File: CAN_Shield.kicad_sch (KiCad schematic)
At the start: 17 parts, among them J1 GPIO, U1 MX128-5.08-09P-GN01-CU-Y-A, U2 MCP2515T-I/SO, U3 MX128-5.08-10P-GN01-CU-Y-A, U4 SN65HVD230DR, X1 X322516MLB4SI

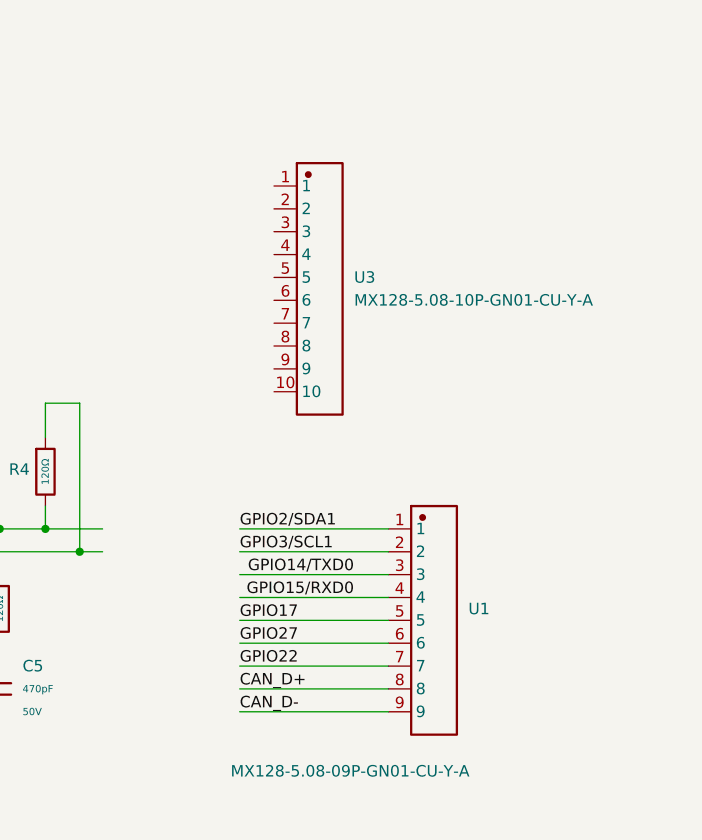
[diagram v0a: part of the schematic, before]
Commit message: change from gpio to gnd at screw terminal and add copper pour for gnd
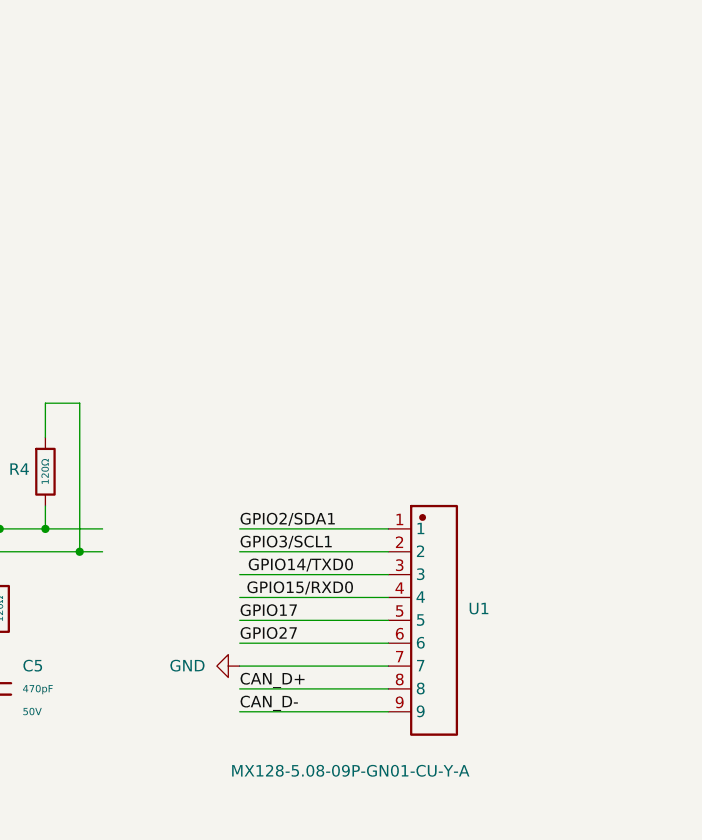
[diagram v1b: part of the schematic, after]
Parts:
- removed U3: MX128-5.08-10P-GN01-CU-Y-A, symbol ImportSymbol:MX128-5.08-10P-GN01-CU-Y-A
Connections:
- net GND: now also U1.7
- net GPIO22: no longer U1.7
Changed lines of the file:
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@@
 	(wire
 		(pts
-			(xy 224.79 139.7) (xy 241.3 139.7)
-		)
-		(stroke
-			(width 0)
-			(type default)
-		)
-	)
-	(wire
-		(pts
 			(xy 203.2 114.3) (xy 203.2 110.49)
 		)
@@
 	(wire
 		(pts
+			(xy 224.79 139.7) (xy 241.3 139.7)
+		)
+		(stroke
+			(width 0)
+			(type default)
+		)
+	)
+	(wire
+		(pts
 			(xy 49.53 44.45) (xy 52.07 44.45)
 		)
@@
 		)
 	)
-	(label "GPIO22"
-		(at 224.79 139.7 0)
-		(effects
-			(font
-				(size 1.27 1.27)
-			)
-			(justify left bottom)
-		)
-	)
 	(label "GPIO23"
 		(at 91.44 52.07 180)
@@
 	)
 	(symbol
+		(lib_name "GND_4")
+		(lib_id "power:GND")
+		(at 224.79 139.7 270)
+		(unit 1)
+		(exclude_from_sim no)
+		(in_bom yes)
+		(on_board yes)
+		(dnp no)
+		(fields_autoplaced yes)
+		(property "Reference" "#PWR6"
+			(at 218.44 139.7 0)
+			(effects
+				(font
+					(size 1.27 1.27)
+				)
+				(hide yes)
+			)
+		)
+		(property "Value" "GND"
+			(at 220.98 139.6999 90)
+			(effects
+				(font
+					(size 1.27 1.27)
+				)
+				(justify right)
+			)
+		)
+		(property "Footprint" ""
+			(at 224.79 139.7 0)
+			(effects
+				(font
+					(size 1.27 1.27)
+				)
+				(hide yes)
+			)
+		)
+		(property "Datasheet" ""
+			(at 224.79 139.7 0)
+			(effects
+				(font
+					(size 1.27 1.27)
+				)
+				(hide yes)
+			)
+		)
+		(property "Description" "Power symbol creates a global label with name \"GND\" , ground"
+			(at 224.79 139.7 0)
+			(effects
+				(font
+					(size 1.27 1.27)
+				)
+				(hide yes)
+			)
+		)
+		(pin "1"
+		)
+		(instances
+			(project "CAN_Shield"
+				(path "/e63e39d7-6ac0-4ffd-8aa3-1841a4541b55"
+					(reference "#PWR6")
+					(unit 1)
+				)
+			)
+		)
+	)
+	(symbol
 		(lib_name "GND_1")
 		(lib_id "power:GND")
@@
 					(unit 1)
 				)
-			)
-		)
-	)
-	(symbol
-		(lib_id "ImportSymbol:MX128-5.08-10P-GN01-CU-Y-A")
-		(at 233.68 97.79 0)
-		(unit 1)
-		(exclude_from_sim no)
-		(in_bom yes)
-		(on_board yes)
-		(dnp no)
-		(fields_autoplaced yes)
-		(property "Reference" "U3"
-			(at 237.49 96.5199 0)
-			(effects
-				(font
-					(size 1.27 1.27)
-				)
-				(justify left)
-			)
-		)
-		(property "Value" "MX128-5.08-10P-GN01-CU-Y-A"
-			(at 237.49 99.0599 0)
-			(effects
-				(font
-					(size 1.27 1.27)
-				)
-				(justify left)
-			)
-		)
-		(property "Footprint" ""
-			(at 233.68 97.79 0)
-			(effects
-				(font
-					(size 1.27 1.27)
-				)
-				(hide yes)
-			)
-		)
-		(property "Datasheet" ""
-			(at 233.68 97.79 0)
-			(effects
-				(font
-					(size 1.27 1.27)
-				)
-				(hide yes)
-			)
-		)
-		(property "Description" ""
-			(at 233.68 97.79 0)
-			(effects
-				(font
-					(size 1.27 1.27)
-				)
-				(hide yes)
-			)
-		)
-		(property "Manufacturer Part" "MX128-5.08-10P-GN01-Cu-Y-A"
-			(at 233.68 97.79 0)
-			(effects
-				(font
-					(size 1.27 1.27)
-				)
-				(hide yes)
-			)
-		)
-		(property "Manufacturer" "MAX(迈旭)"
-			(at 233.68 97.79 0)
-			(effects
-				(font
-					(size 1.27 1.27)
-				)
-				(hide yes)
-			)
-		)
-		(property "Supplier Part" "C5290383"
-			(at 233.68 97.79 0)
-			(effects
-				(font
-					(size 1.27 1.27)
-				)
-				(hide yes)
-			)
-		)
-		(property "Supplier" "LCSC"
-			(at 233.68 97.79 0)
-			(effects
-				(font
-					(size 1.27 1.27)
-				)
-				(hide yes)
-			)
-		)
-		(pin "3"
-		)
-		(pin "10"
-		)
-		(pin "6"
-		)
-		(pin "1"
-		)
-		(pin "2"
-		)
-		(pin "9"
-		)
-		(pin "5"
-		)
-		(pin "4"
-		)
-		(pin "7"
-		)
-		(pin "8"
-		)
-		(instances
-			(project ""
-				(path "/e63e39d7-6ac0-4ffd-8aa3-1841a4541b55"
-					(reference "U3")
-					(unit 1)
-				)

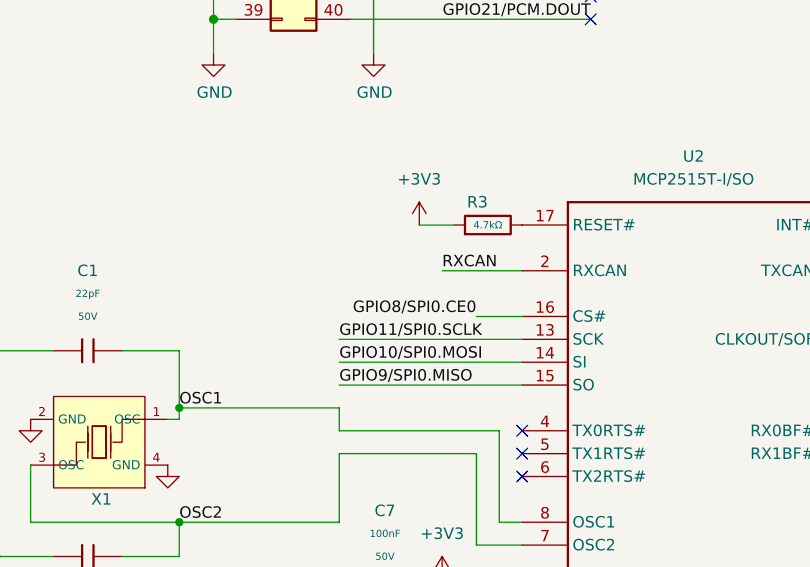
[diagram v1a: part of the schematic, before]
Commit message: change can diff pair trace width to 0.35 mm get 133ohm zdiff
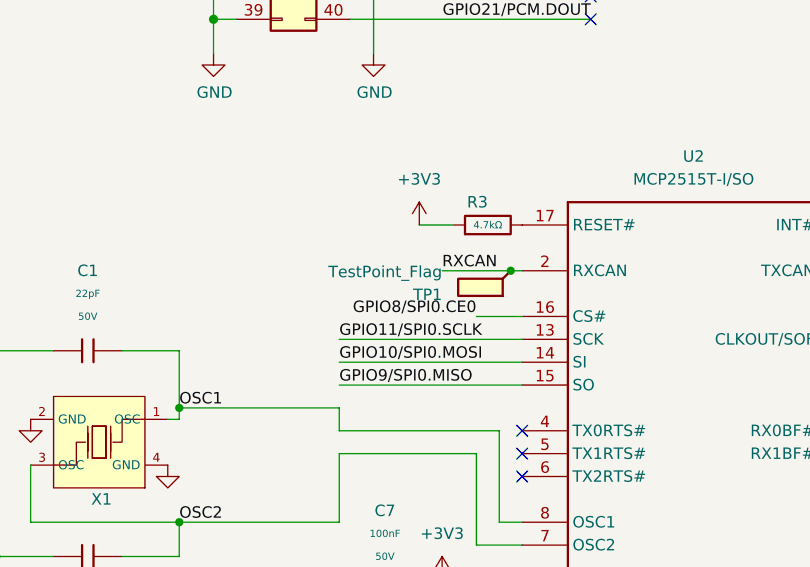
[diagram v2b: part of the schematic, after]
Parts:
- added TP1: TestPoint_Flag, TestPoint:TestPoint_Pad_3.0x3.0mm, symbol Connector:TestPoint_Flag
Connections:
- net RXCAN: now also TP1.1
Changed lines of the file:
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@@
 	)
 	(junction
+		(at 82.55 110.49)
+		(diameter 0)
+		(color 0 0 0 0)
+	)
+	(junction
 		(at 49.53 82.55)
 		(diameter 1.016)
@@
 	(wire
 		(pts
+			(xy 82.55 110.49) (xy 83.82 110.49)
+		)
+		(stroke
+			(width 0)
+			(type default)
+		)
+	)
+	(wire
+		(pts
 			(xy 46.99 19.05) (xy 46.99 34.29)
 		)
@@
 	(wire
 		(pts
-			(xy 74.93 110.49) (xy 83.82 110.49)
+			(xy 74.93 110.49) (xy 82.55 110.49)
 		)
 		(stroke
@@
 					(unit 1)
 				)
+			)
+		)
+	)
+	(symbol
+		(lib_id "Connector:TestPoint_Flag")
+		(at 82.55 110.49 180)
+		(unit 1)
+		(exclude_from_sim no)
+		(in_bom yes)
+		(on_board yes)
+		(dnp no)
+		(property "Reference" "TP1"
+			(at 74.93 113.1571 0)
+			(effects
+				(font
+					(size 1.27 1.27)
+				)
+				(justify left)
+			)
+		)
+		(property "Value" "TestPoint_Flag"
+			(at 74.93 110.6171 0)
+			(effects
+				(font
+					(size 1.27 1.27)
+				)
+				(justify left)
+			)
+		)
+		(property "Footprint" "TestPoint:TestPoint_Pad_3.0x3.0mm"
+			(at 77.47 110.49 0)
+			(effects
+				(font
+					(size 1.27 1.27)
+				)
+				(hide yes)
+			)
+		)
+		(property "Datasheet" "~"
+			(at 77.47 110.49 0)
+			(effects
+				(font
+					(size 1.27 1.27)
+				)
+				(hide yes)
+			)
+		)
+		(property "Description" "test point (alternative flag-style design)"
+			(at 82.55 110.49 0)
+			(effects
+				(font
+					(size 1.27 1.27)
+				)
+				(hide yes)
+			)
+		)
+		(pin "1"
+		)
+		(instances
+			(project ""
+				(path "/e63e39d7-6ac0-4ffd-8aa3-1841a4541b55"
+					(reference "TP1")
+					(unit 1)
+				)

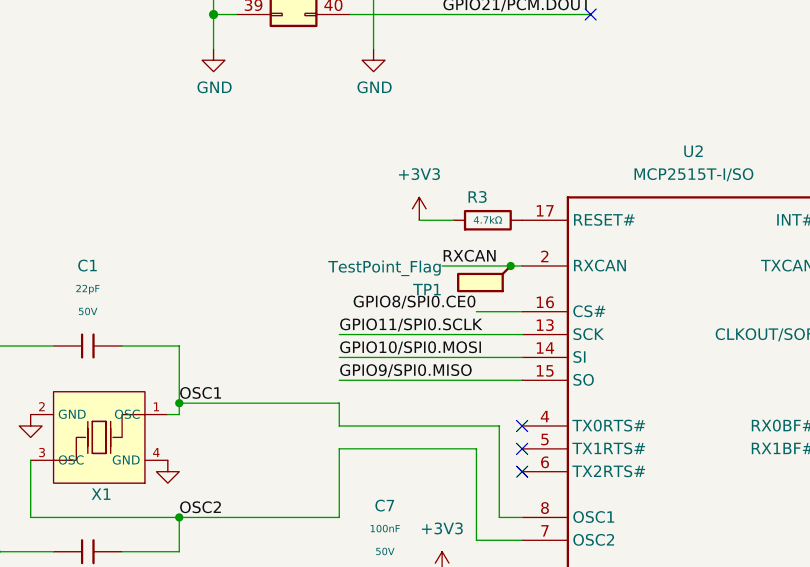
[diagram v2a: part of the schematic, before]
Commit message: tune CAN diff pair skew
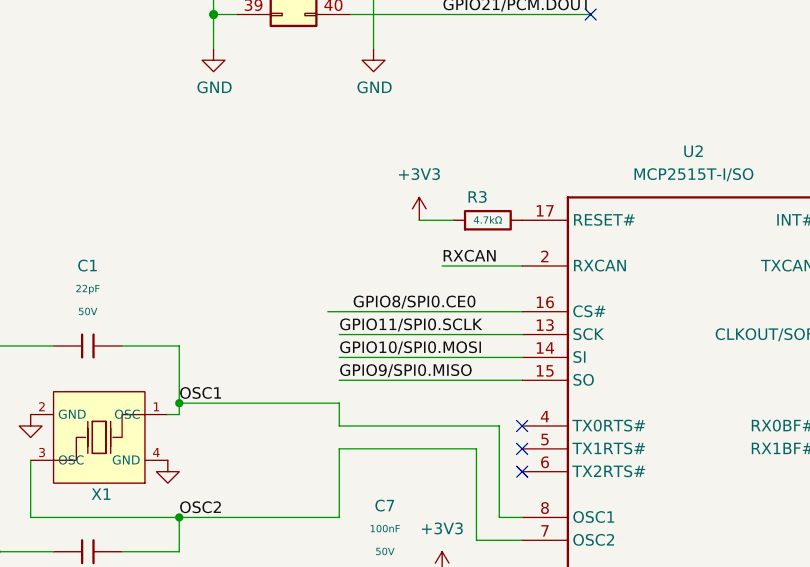
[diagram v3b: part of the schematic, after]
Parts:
- removed TP1: TestPoint_Flag, TestPoint:TestPoint_Pad_3.0x3.0mm, symbol Connector:TestPoint_Flag
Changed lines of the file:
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@@
 	)
 	(junction
-		(at 82.55 110.49)
-		(diameter 0)
-		(color 0 0 0 0)
-	)
-	(junction
 		(at 49.53 82.55)
 		(diameter 1.016)
@@
 	(wire
 		(pts
-			(xy 67.31 69.85) (xy 67.31 74.93)
+			(xy 121.92 110.49) (xy 125.73 110.49)
 		)
 		(stroke
 			(width 0)
-			(type solid)
+			(type default)
 		)
 	)
 	(wire
 		(pts
-			(xy 224.79 137.16) (xy 241.3 137.16)
+			(xy 67.31 69.85) (xy 67.31 74.93)
 		)
 		(stroke
 			(width 0)
-			(type default)
+			(type solid)
 		)
 	)
 	(wire
 		(pts
-			(xy 82.55 110.49) (xy 83.82 110.49)
+			(xy 224.79 137.16) (xy 241.3 137.16)
 		)
 		(stroke
@@
 	(wire
 		(pts
-			(xy 74.93 110.49) (xy 82.55 110.49)
+			(xy 74.93 110.49) (xy 83.82 110.49)
 		)
 		(stroke
@@
 	(wire
 		(pts
-			(xy 121.92 110.49) (xy 125.73 110.49)
-		)
-		(stroke
-			(width 0)
-			(type default)
-		)
-	)
-	(wire
-		(pts
 			(xy 22.86 41.91) (xy 52.07 41.91)
 		)
@@
 	(wire
 		(pts
-			(xy 78.74 115.57) (xy 83.82 115.57)
-		)
-		(stroke
-			(width 0)
-			(type default)
-		)
-	)
-	(wire
-		(pts
 			(xy 22.86 72.39) (xy 52.07 72.39)
 		)
@@
 	(wire
 		(pts
+			(xy 62.23 115.57) (xy 83.82 115.57)
+		)
+		(stroke
+			(width 0)
+			(type default)
+		)
+	)
+	(wire
+		(pts
 			(xy 198.12 137.16) (xy 198.12 138.43)
 		)
@@
 					(unit 1)
 				)
-			)
-		)
-	)
-	(symbol
-		(lib_id "Connector:TestPoint_Flag")
-		(at 82.55 110.49 180)
-		(unit 1)
-		(exclude_from_sim no)
-		(in_bom yes)
-		(on_board yes)
-		(dnp no)
-		(property "Reference" "TP1"
-			(at 74.93 113.1571 0)
-			(effects
-				(font
-					(size 1.27 1.27)
-				)
-				(justify left)
-			)
-		)
-		(property "Value" "TestPoint_Flag"
-			(at 74.93 110.6171 0)
-			(effects
-				(font
-					(size 1.27 1.27)
-				)
-				(justify left)
-			)
-		)
-		(property "Footprint" "TestPoint:TestPoint_Pad_3.0x3.0mm"
-			(at 77.47 110.49 0)
-			(effects
-				(font
-					(size 1.27 1.27)
-				)
-				(hide yes)
-			)
-		)
-		(property "Datasheet" "~"
-			(at 77.47 110.49 0)
-			(effects
-				(font
-					(size 1.27 1.27)
-				)
-				(hide yes)
-			)
-		)
-		(property "Description" "test point (alternative flag-style design)"
-			(at 82.55 110.49 0)
-			(effects
-				(font
-					(size 1.27 1.27)
-				)
-				(hide yes)
-			)
-		)
-		(pin "1"
-		)
-		(instances
-			(project ""
-				(path "/e63e39d7-6ac0-4ffd-8aa3-1841a4541b55"
-					(reference "TP1")
-					(unit 1)
-				)

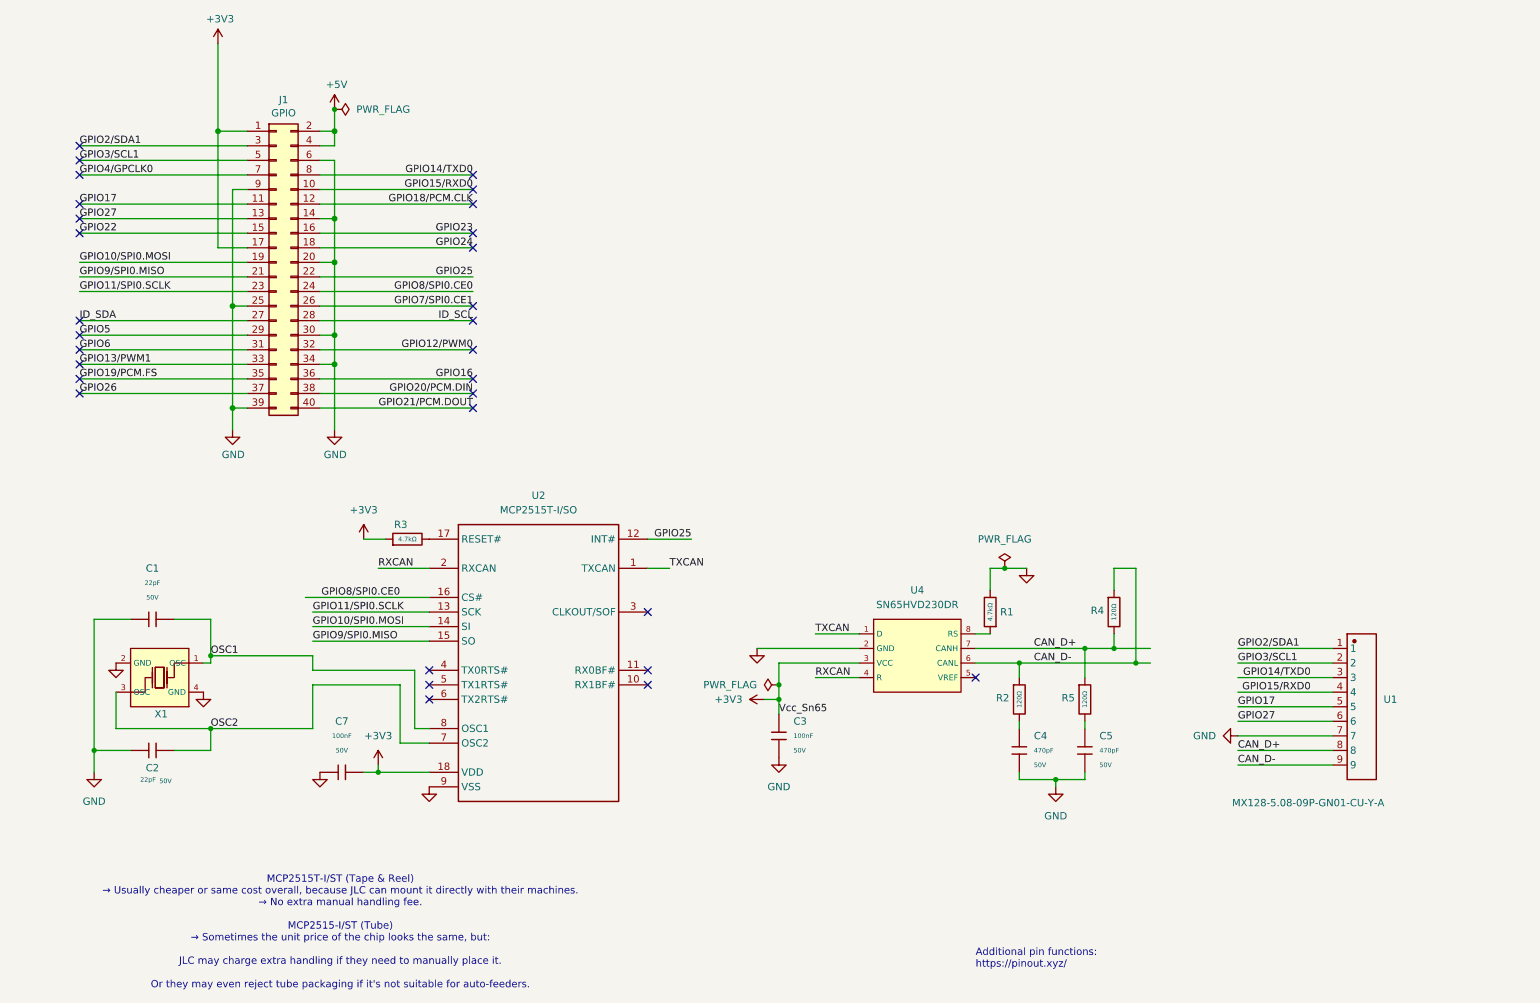
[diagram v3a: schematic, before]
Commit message: quickly add 4 pin screw terminal block for I2C and move old SDA and SCL to new screw terminal block
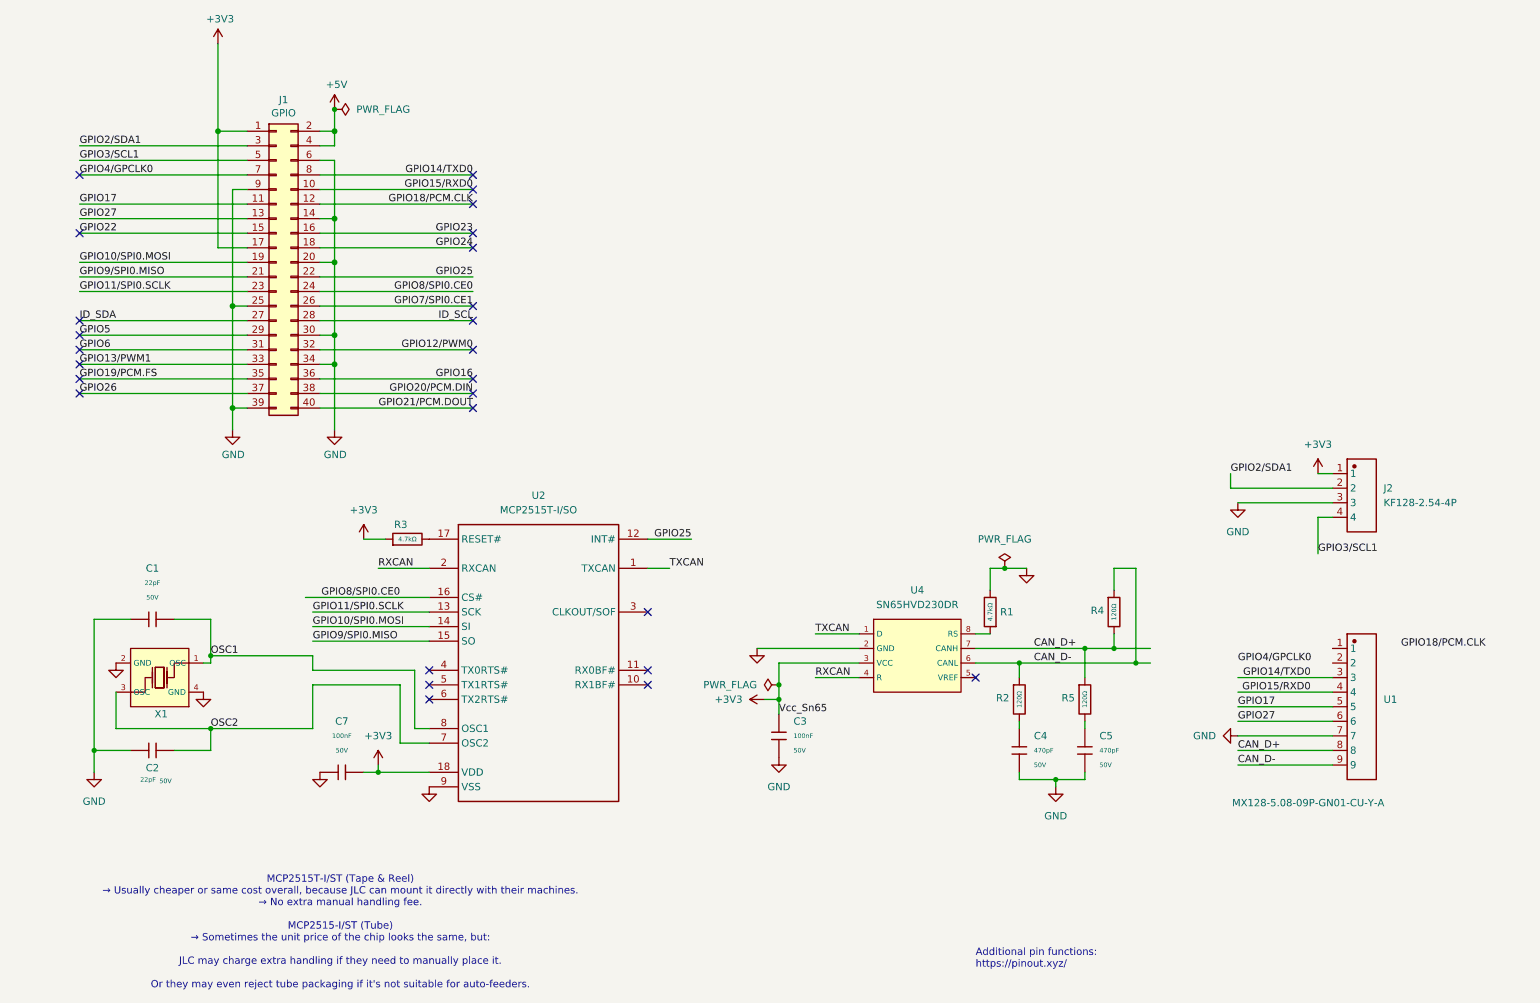
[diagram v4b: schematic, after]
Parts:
- added J2: KF128-2.54-4P, ImportFP:CONN-TH_4P-P2.54_KF128-2.54-4P, symbol ImportSymbol:KF128-2.54-4P
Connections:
- net +3V3: now also J2.1
- net GND: now also J2.3
- net GPIO2/SDA1: now also J2.2; no longer U1.1
- net GPIO3/SCL1: now also J2.4; no longer U1.2
- no-connect marks 30 -> 26
